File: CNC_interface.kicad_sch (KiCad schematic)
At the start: 25 parts, among them J1 Conn_01x04_Male, J10 Conn_01x08, J11 Conn_01x08, J12 Conn_01x08, J13 Conn_01x08, J14 Conn_01x03_Male, J15 Conn_01x03_Male, J16 Conn_01x03_Male, J2 Conn_01x04_Male, J3 Conn_01x04_Male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

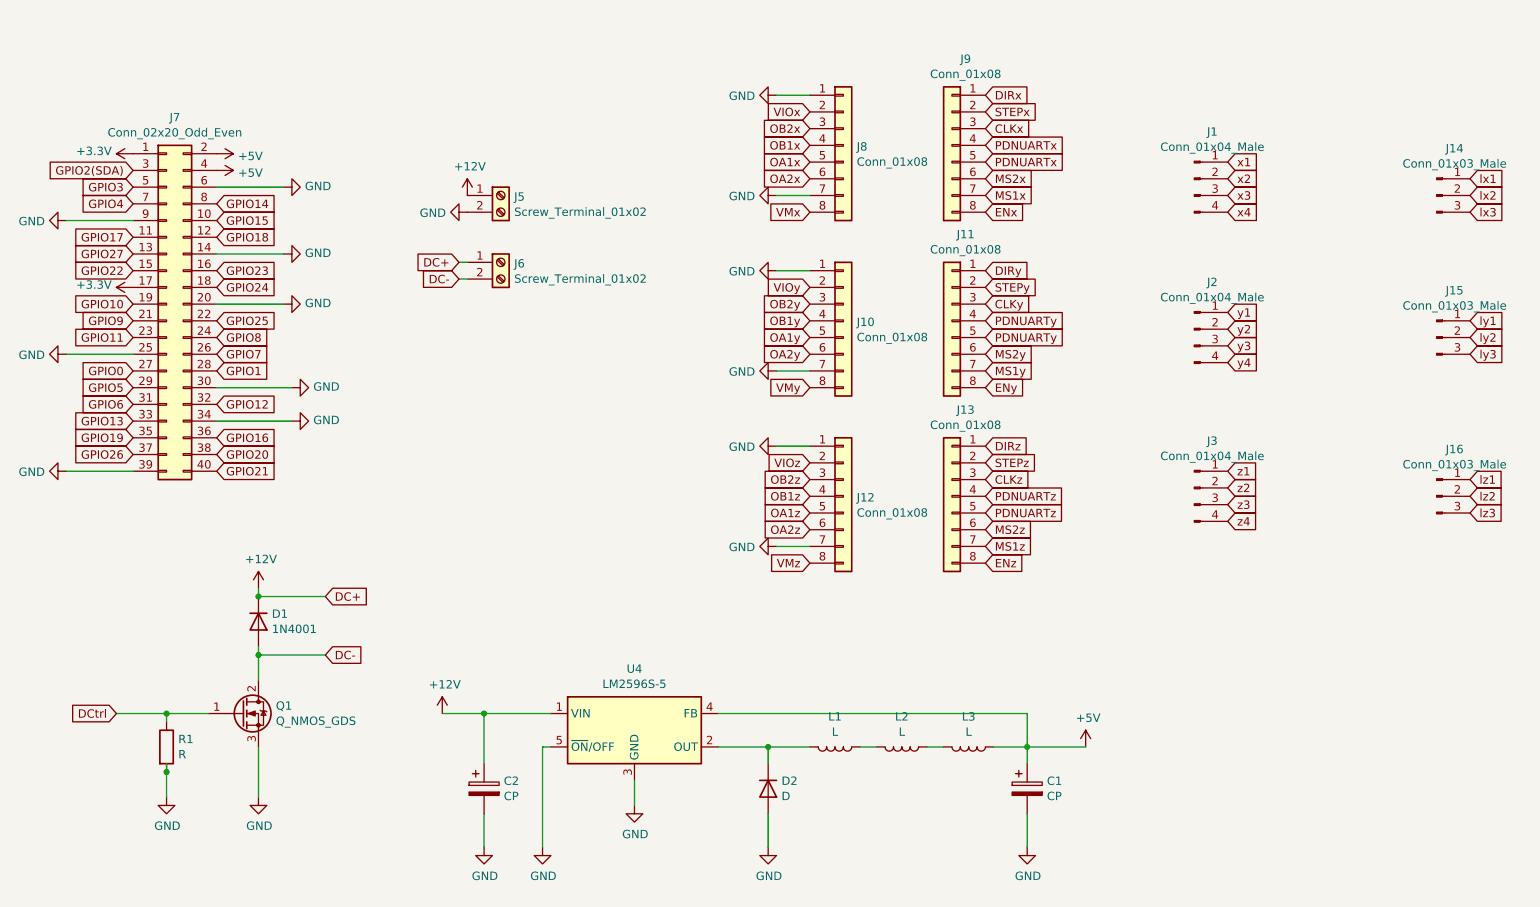
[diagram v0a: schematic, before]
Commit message: Adding jumper Arduino
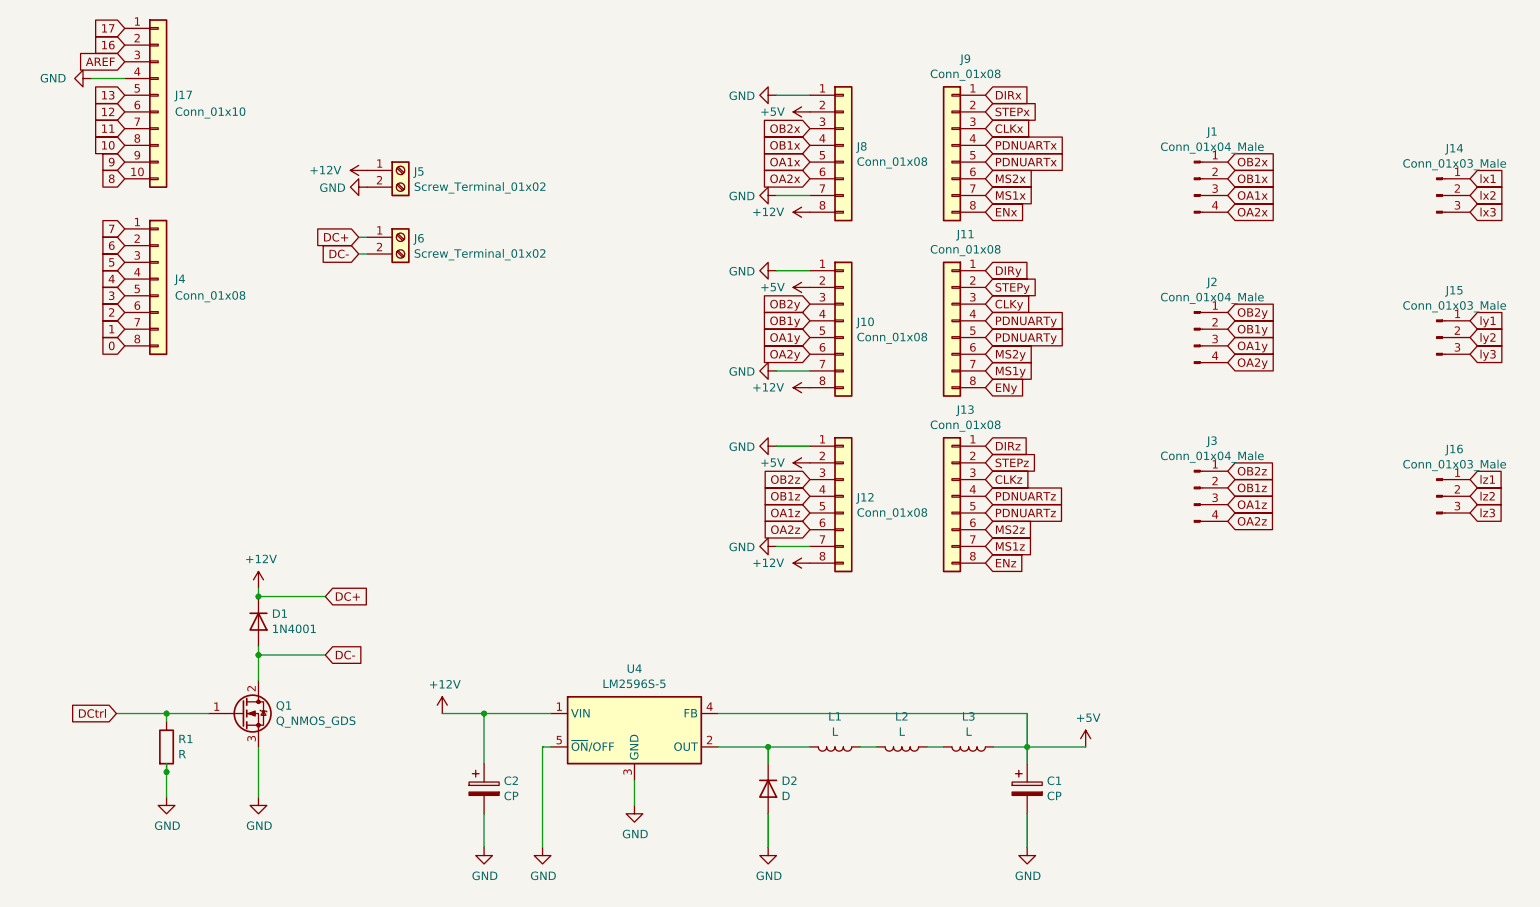
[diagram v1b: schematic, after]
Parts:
- removed J7: Conn_02x20_Odd_Even, Connector_PinSocket_2.54mm:PinSocket_2x20_P2.54mm_Vertical, symbol Connector_Generic:Conn_02x20_Odd_Even
- added J17: Conn_01x10, Connector_PinSocket_2.54mm:PinSocket_1x10_P2.54mm_Horizontal, symbol Connector_Generic:Conn_01x10
- added J4: Conn_01x08, Connector_PinSocket_2.54mm:PinSocket_1x08_P2.54mm_Horizontal, symbol Connector_Generic:Conn_01x08
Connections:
- net VIOx is gone; now on net +5V: J8.2 (Pin_2)
- net VIOy is gone; now on net +5V: J10.2 (Pin_2)
- net VIOz is gone; now on net +5V: J12.2 (Pin_2)
- net VMx is gone; now on net +12V: J8.8 (Pin_8)
- net VMy is gone; now on net +12V: J10.8 (Pin_8)
- net VMz is gone; now on net +12V: J12.8 (Pin_8)
- net x1 is gone; now on net OB2x: J1.1 (Pin_1)
- net x2 is gone; now on net OB1x: J1.2 (Pin_2)
- net x3 is gone; now on net OA1x: J1.3 (Pin_3)
- net x4 is gone; now on net OA2x: J1.4 (Pin_4)
- net y1 is gone; now on net OB2y: J2.1 (Pin_1)
- net y2 is gone; now on net OB1y: J2.2 (Pin_2)
- net y3 is gone; now on net OA1y: J2.3 (Pin_3)
- net y4 is gone; now on net OA2y: J2.4 (Pin_4)
- net z1 is gone; now on net OB2z: J3.1 (Pin_1)
- net z2 is gone; now on net OB1z: J3.2 (Pin_2)
- net z3 is gone; now on net OA1z: J3.3 (Pin_3)
- net z4 is gone; now on net OA2z: J3.4 (Pin_4)
- net GND: now also J17.4 (Pin_4)
- new net 0: J4.8 (Pin_8)
- new net 1: J4.7 (Pin_7)
- new net 10: J17.8 (Pin_8)
- new net 11: J17.7 (Pin_7)
- new net 12: J17.6 (Pin_6)
- new net 13: J17.5 (Pin_5)
- new net 16: J17.2 (Pin_2)
- new net 17: J17.1 (Pin_1)
- new net 2: J4.6 (Pin_6)
- new net 3: J4.5 (Pin_5)
- new net 4: J4.4 (Pin_4)
- new net 5: J4.3 (Pin_3)
- new net 6: J4.2 (Pin_2)
- new net 7: J4.1 (Pin_1)
- new net 8: J17.10 (Pin_10)
- new net 9: J17.9 (Pin_9)
- new net AREF: J17.3 (Pin_3)
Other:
- moved on the sheet: J5, J6

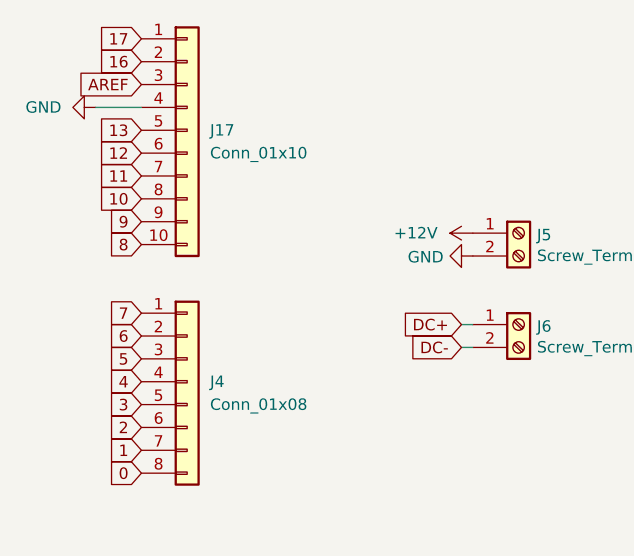
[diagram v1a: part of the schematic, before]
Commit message: Placing components on PCB
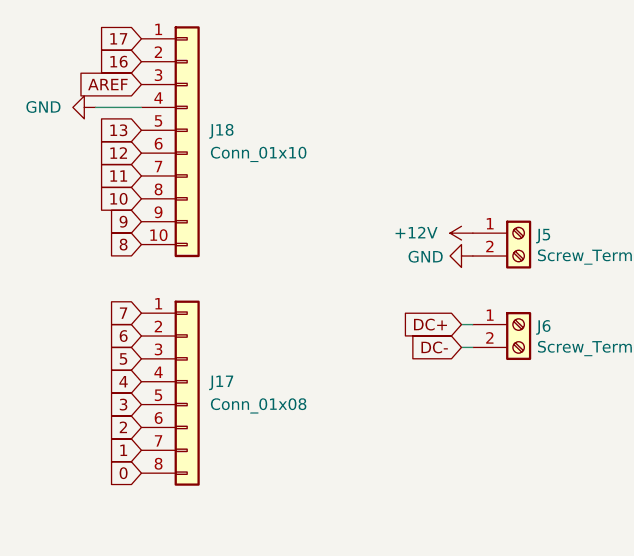
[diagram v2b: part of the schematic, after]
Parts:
- renumbered J4 to J17, J17 to J18
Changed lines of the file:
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@@
   (symbol (lib_id "Connector_Generic:Conn_01x08") (at 49.53 60.96 0) (unit 1)
     (in_bom yes) (on_board yes) (fields_autoplaced)
-    (property "Reference" "J4" (id 0) (at 52.07 60.9599 0)
+    (property "Reference" "J17" (id 0) (at 52.07 60.9599 0)
       (effects (font (size 1.27 1.27)) (justify left))
     )
@@
   (symbol (lib_id "power:GND") (at 39.37 30.48 270) (unit 1)
     (in_bom yes) (on_board yes) (fields_autoplaced)
-    (property "Reference" "#PWR?" (id 0) (at 33.02 30.48 0)
+    (property "Reference" "#PWR0109" (id 0) (at 33.02 30.48 0)
       (effects (font (size 1.27 1.27)) hide)
     )
@@
   (symbol (lib_id "Connector_Generic:Conn_01x10") (at 49.53 33.02 0) (unit 1)
     (in_bom yes) (on_board yes) (fields_autoplaced)
-    (property "Reference" "J17" (id 0) (at 52.07 33.0199 0)
+    (property "Reference" "J18" (id 0) (at 52.07 33.0199 0)
       (effects (font (size 1.27 1.27)) (justify left))
     )
@@
       (reference "#PWR0108") (unit 1) (value "GND") (footprint "")
     )
+    (path "/63a7cf3f-abce-42fb-b778-80e472f2ad88"
+      (reference "#PWR0109") (unit 1) (value "GND") (footprint "")
+    )
     (path "/00000000-0000-0000-0000-0000620756d9"
       (reference "#PWR0121") (unit 1) (value "GND") (footprint "")
@@
       (reference "#PWR0136") (unit 1) (value "+12V") (footprint "")
     )
-    (path "/63a7cf3f-abce-42fb-b778-80e472f2ad88"
-      (reference "#PWR?") (unit 1) (value "GND") (footprint "")
-    )
     (path "/00000000-0000-0000-0000-000062089e0f"
       (reference "C1") (unit 1) (value "CP") (footprint "Capacitor_THT:CP_Radial_D8.0mm_P3.50mm")
@@
       (reference "J3") (unit 1) (value "Conn_01x04_Male") (footprint "Connector_JST:JST_XH_B4B-XH-A_1x04_P2.50mm_Vertical")
     )
-    (path "/5c464a80-ff5d-4b0d-bc26-7c85ac545cdf"
-      (reference "J4") (unit 1) (value "Conn_01x08") (footprint "Connector_PinSocket_2.54mm:PinSocket_1x08_P2.54mm_Horizontal")
-    )
     (path "/00000000-0000-0000-0000-00006208728f"
       (reference "J5") (unit 1) (value "Screw_Terminal_01x02") (footprint "CNC_interface:TerminalBlock_Phoenix_MKDSP-1,5-2-5.08_1x02_P5.08mm")
@@
       (reference "J16") (unit 1) (value "Conn_01x03_Male") (footprint "Connector_JST:JST_XH_B3B-XH-A_1x03_P2.50mm_Vertical")
     )
+    (path "/5c464a80-ff5d-4b0d-bc26-7c85ac545cdf"
+      (reference "J17") (unit 1) (value "Conn_01x08") (footprint "Connector_PinSocket_2.54mm:PinSocket_1x08_P2.54mm_Horizontal")
+    )
     (path "/8ef7ca08-78ca-4fb4-8425-fbabd0d4a909"
-      (reference "J17") (unit 1) (value "Conn_01x10") (footprint "Connector_PinSocket_2.54mm:PinSocket_1x10_P2.54mm_Horizontal")
+      (reference "J18") (unit 1) (value "Conn_01x10") (footprint "Connector_PinSocket_2.54mm:PinSocket_1x10_P2.54mm_Horizontal")
     )
     (path "/00000000-0000-0000-0000-000062097f6a"

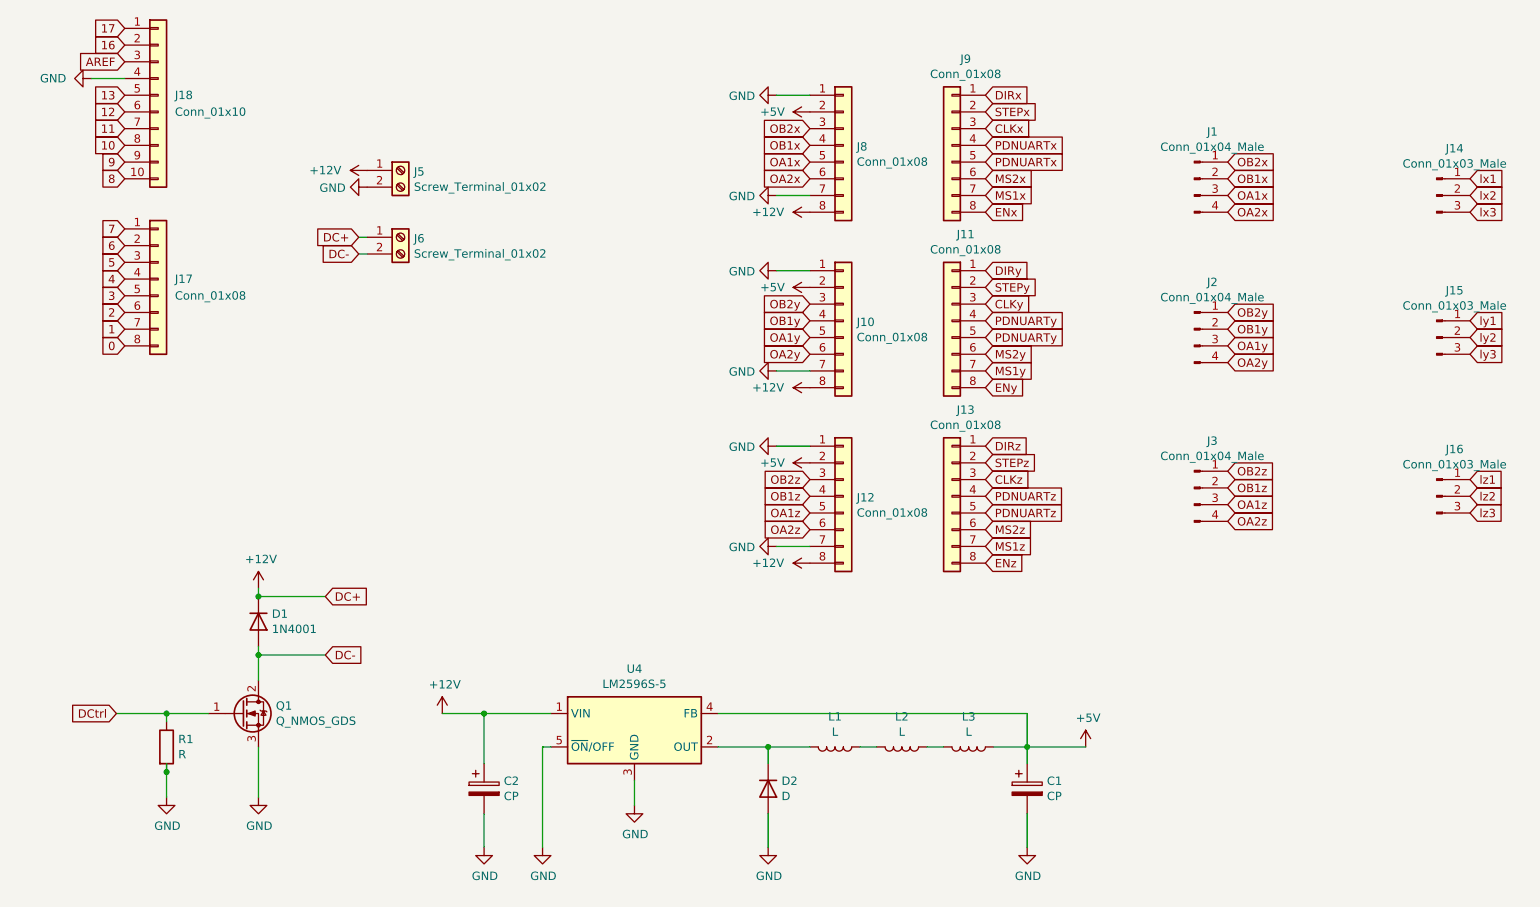
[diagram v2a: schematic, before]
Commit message: wiring input to TMC
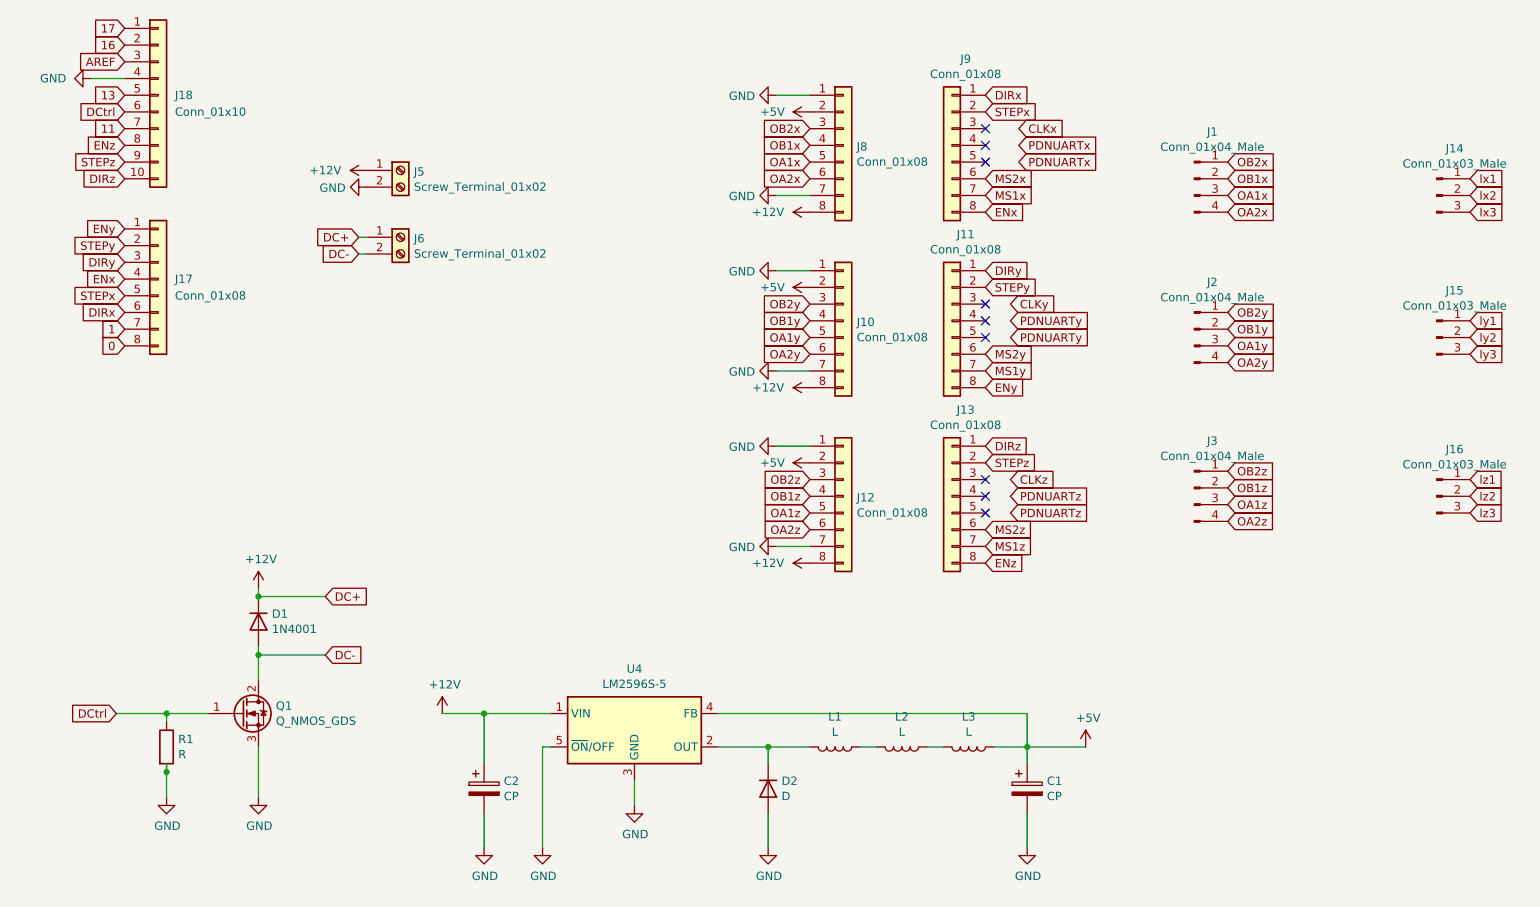
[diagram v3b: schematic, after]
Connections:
- net 10 is gone; now on net ENz: J18.8 (Pin_8)
- net 12 is gone; now on net DCtrl: J18.6 (Pin_6)
- net 2 is gone; now on net DIRx: J17.6 (Pin_6)
- net 3 is gone; now on net STEPx: J17.5 (Pin_5)
- net 4 is gone; now on net ENx: J17.4 (Pin_4)
- net 5 is gone; now on net DIRy: J17.3 (Pin_3)
- net 6 is gone; now on net STEPy: J17.2 (Pin_2)
- net 7 is gone; now on net ENy: J17.1 (Pin_1)
- net 8 is gone; now on net DIRz: J18.10 (Pin_10)
- net 9 is gone; now on net STEPz: J18.9 (Pin_9)
- net CLKx: no longer J9.3 (Pin_3)
- net CLKy: no longer J11.3 (Pin_3)
- net CLKz: no longer J13.3 (Pin_3)
- net PDNUARTx: no longer J9.4 (Pin_4), J9.5 (Pin_5)
- net PDNUARTy: no longer J11.4 (Pin_4), J11.5 (Pin_5)
- net PDNUARTz: no longer J13.4 (Pin_4), J13.5 (Pin_5)
- no-connect marks 0 -> 9

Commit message: debut seance
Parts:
- added J19: USB_C_Receptacle, Connector_USB:USB_C_Receptacle_Amphenol_12401548E4-2A_CircularHoles, symbol Connector:USB_C_Receptacle
- D2: footprint (none) -> Diode_THT:D_DO-201AD_P15.24mm_Horizontal
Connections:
- net 11 is gone; now on net ENz: J18.7 (Pin_7)
- net lx1 is gone; now on net +5V: J14.1 (Pin_1)
- net lx2 is gone; now on net GND: J14.2 (Pin_2)
- net ly1 is gone; now on net +5V: J15.1 (Pin_1)
- net ly2 is gone; now on net GND: J15.2 (Pin_2)
- net ly3 is gone; now on net Ly: J15.3 (Pin_3)
- net lz1 is gone; now on net +5V: J16.1 (Pin_1)
- net lz2 is gone; now on net GND: J16.2 (Pin_2)
- net lz3 is gone; now on net Lz: J16.3 (Pin_3)
- net +5V: now also J19.A4 (VBUS), J19.A9 (VBUS), J19.B4 (VBUS), J19.B9 (VBUS)
- net DIRx: now also J17.5 (Pin_5); no longer J17.6 (Pin_6)
- net DIRy: now also J17.2 (Pin_2); no longer J17.3 (Pin_3)
- net DIRz: now also J18.9 (Pin_9); no longer J18.10 (Pin_10)
- net ENx: now also J17.3 (Pin_3); no longer J17.4 (Pin_4)
- net ENy: now also J18.10 (Pin_10); no longer J17.1 (Pin_1)
- net ENz: no longer J18.8 (Pin_8)
- net GND: now also J19.A1 (GND), J19.A12 (GND), J19.B1 (GND), J19.B12 (GND), J19.S1 (SHIELD)
- net STEPx: now also J17.4 (Pin_4); no longer J17.5 (Pin_5)
- net STEPy: now also J17.1 (Pin_1); no longer J17.2 (Pin_2)
- net STEPz: now also J18.8 (Pin_8); no longer J18.9 (Pin_9)
- net 0 renamed Lz
- net 1 renamed Ly
- net lx3 renamed Lx
- net Lx: now also J17.6 (Pin_6)
- no-connect marks 9 -> 25
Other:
- moved on the sheet: D1, J17, J18, J5, J6, Q1, R1
